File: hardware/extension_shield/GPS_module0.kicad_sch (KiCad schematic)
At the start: 1 part, among them U2 NEO-7M-MODULE

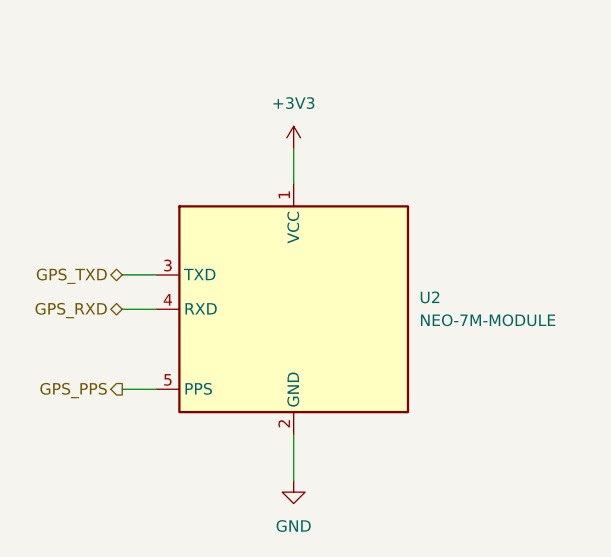
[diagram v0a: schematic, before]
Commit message: [HW] Adds Labels To Expansion Shield Schematic, PDF Schematic & Performed Schematic, PCB Tests.
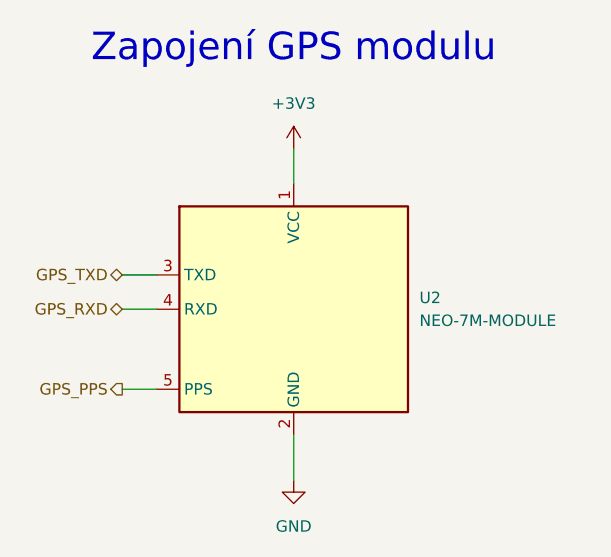
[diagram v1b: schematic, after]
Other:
- note added: "Zapojení GPS modulu"
- title: Datalogger Expansion Shield -> Data Logger Expansion Shield
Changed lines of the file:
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@@
 	(paper "A4")
 	(title_block
-		(title "Datalogger Expansion Shield")
+		(title "Data Logger Expansion Shield")
 		(date "2025-02-26")
 		(rev "1.2")
@@
 		)
 	)
+	(text "Zapojení GPS modulu"
+		(exclude_from_sim no)
+		(at 199.39 66.294 0)
+		(effects
+			(font
+				(size 3.048 3.048)
+			)
+		)
+	)
